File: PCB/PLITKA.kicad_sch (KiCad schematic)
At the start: 55 parts, among them SW1 MX_SW_HS, SW10 MX_SW_HS, SW11 MX_SW_HS, SW12 MX_SW_HS, SW13 MX_SW_HS, SW14 MX_SW_HS, SW15 MX_SW_HS, SW16 MX_SW_HS, SW17 MX_SW_HS, SW18 RotaryEncoder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

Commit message: Metadata corrections
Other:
- title: PLITKA split keyboard -> PLITKA keyboard
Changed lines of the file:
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@@
 	(paper "A5")
 	(title_block
-		(title "PLITKA split keyboard")
-		(date "2022-05-19")
-		(rev "0.2")
-		(comment 1 "Author: GEIST")
+		(title "PLITKA keyboard")
+		(date "12/06/2026")
+		(rev "0.1")
+		(comment 1 "Author: rawrex")
 	)
 	(text "SWITCHMATRIX"

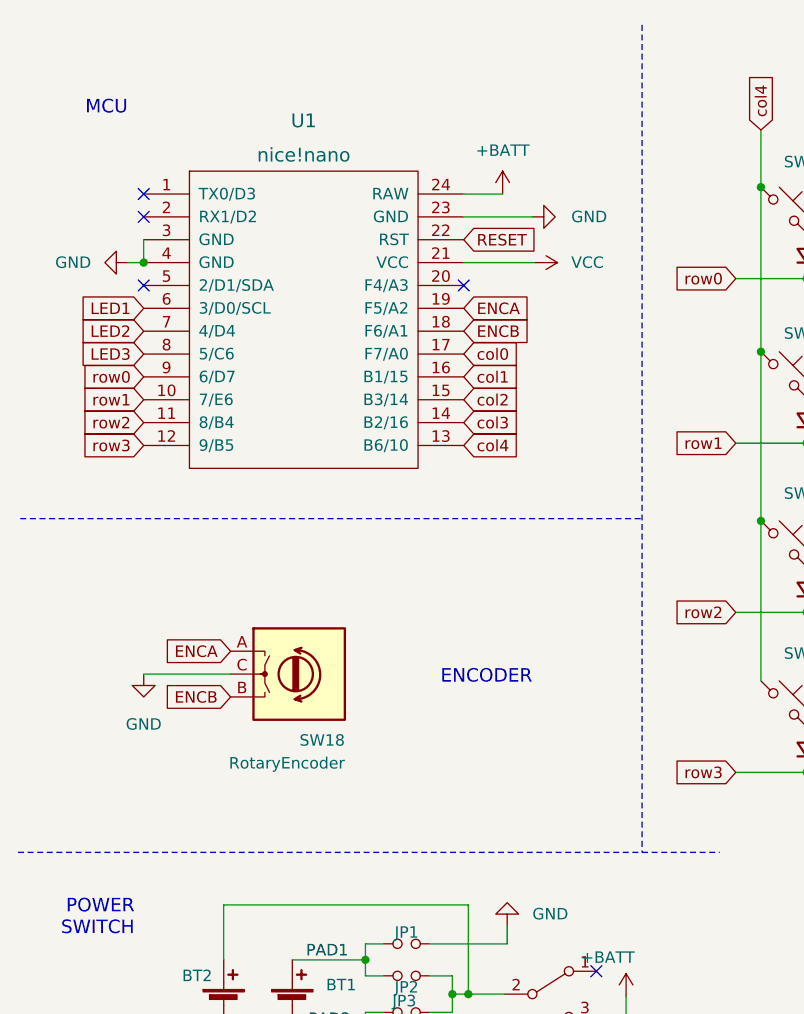
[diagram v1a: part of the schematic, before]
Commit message: Encoder removal
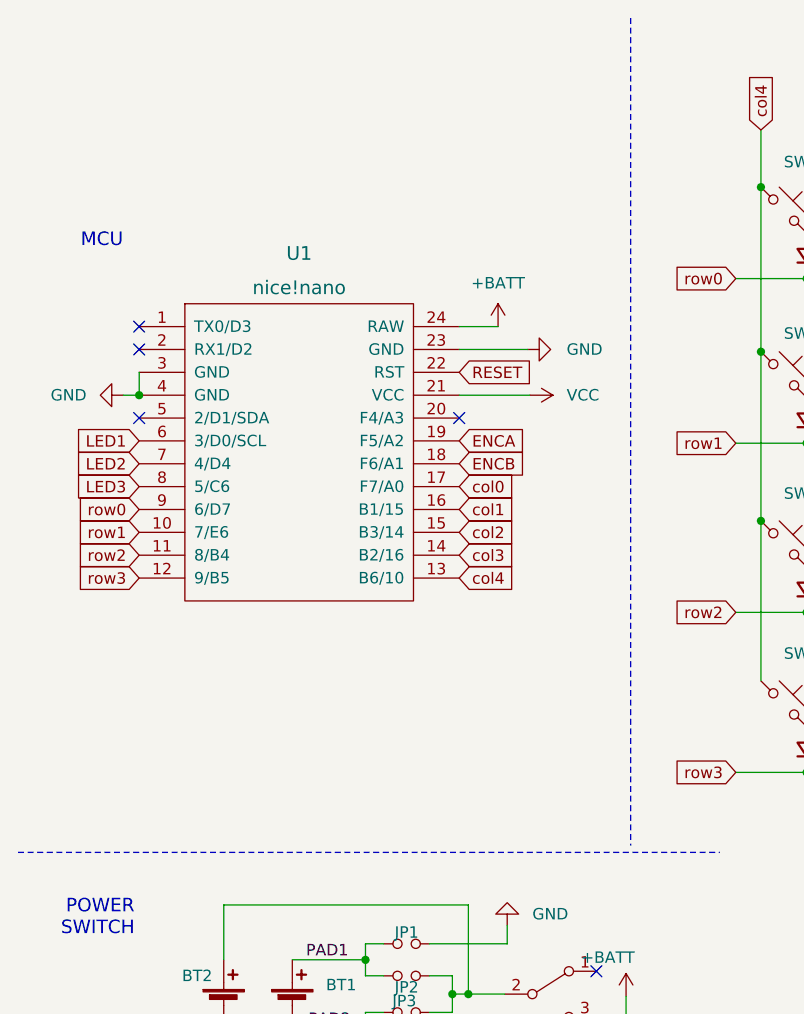
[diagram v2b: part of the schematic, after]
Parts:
- removed SW18: RotaryEncoder, Rotary_Encoder:RotaryEncoder_Alps_EC12E_Vertical_H20mm, symbol Device:RotaryEncoder
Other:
- note removed: "ENCODER"
- moved on the sheet: U1
